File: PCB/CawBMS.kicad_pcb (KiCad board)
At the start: 4 copper layers, 53.5 x 38 mm, 132 parts, among them CN1 SWD, CN2 I2C, CN3 SPI, CN4 USART, CN5 SWD, CN6 WAFER-SH1.0-6PWB, Q1 CSD13381F4, Q10 TP0610K-T1-GE3, Q2 CSD13381F4, Q3 CSD13381F4, Q4 CSD13381F4, Q5 CSD13381F4, Q6 BSC0702LS, Q7 BSC0702LS, Q8 BSC0702LS, Q9 BSC0702LS, SW1 B3U-1000P, SW2 B3U-1000P, SW3 B3U-1000P, U1 STM32F103CBTx, U2 TCAN1044DRBRQ1, U3 TPS61240DRVR, U4 BQ7692003PW, U5 CAN, X1 Crystal_16MHz_15pF_3P

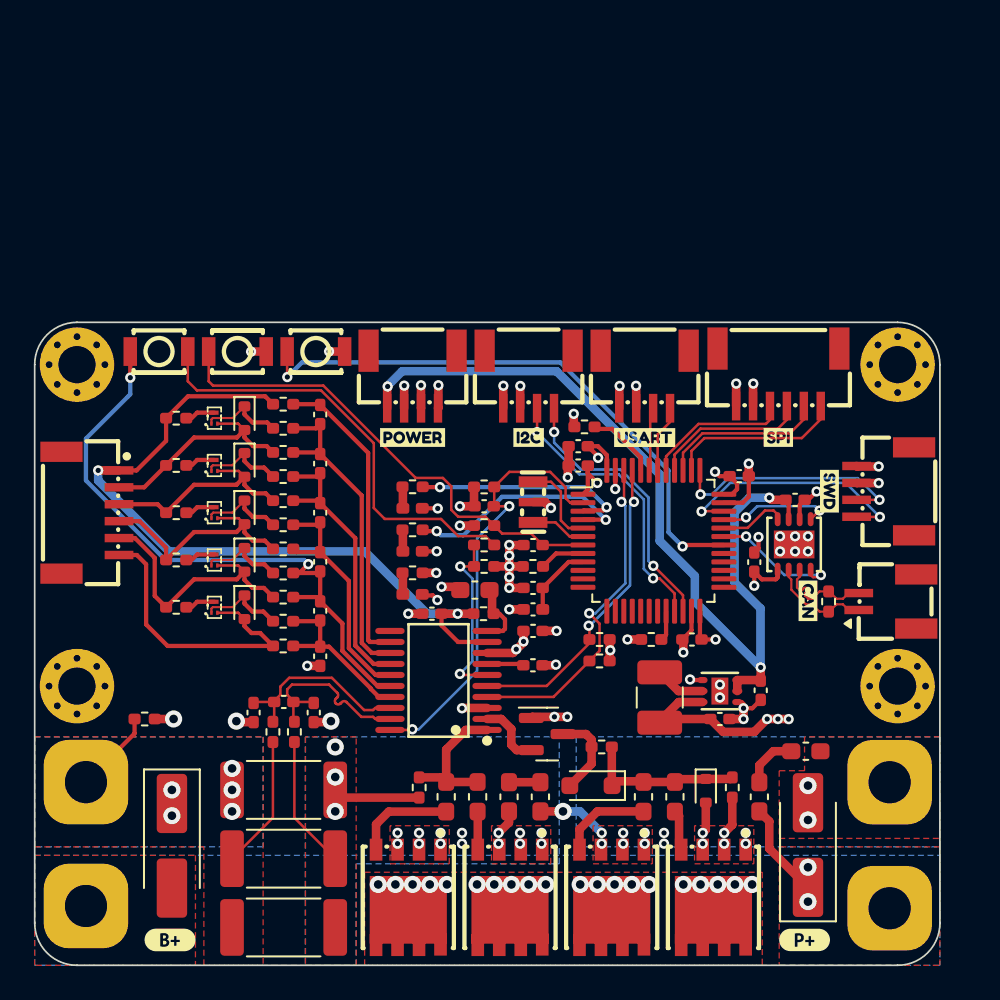
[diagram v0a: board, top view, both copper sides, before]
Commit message: feat(PCB): 新增预充功能; 支持2路电池温度采样; 支持低功耗模式; 更换主控芯片; 采用降压输出5V
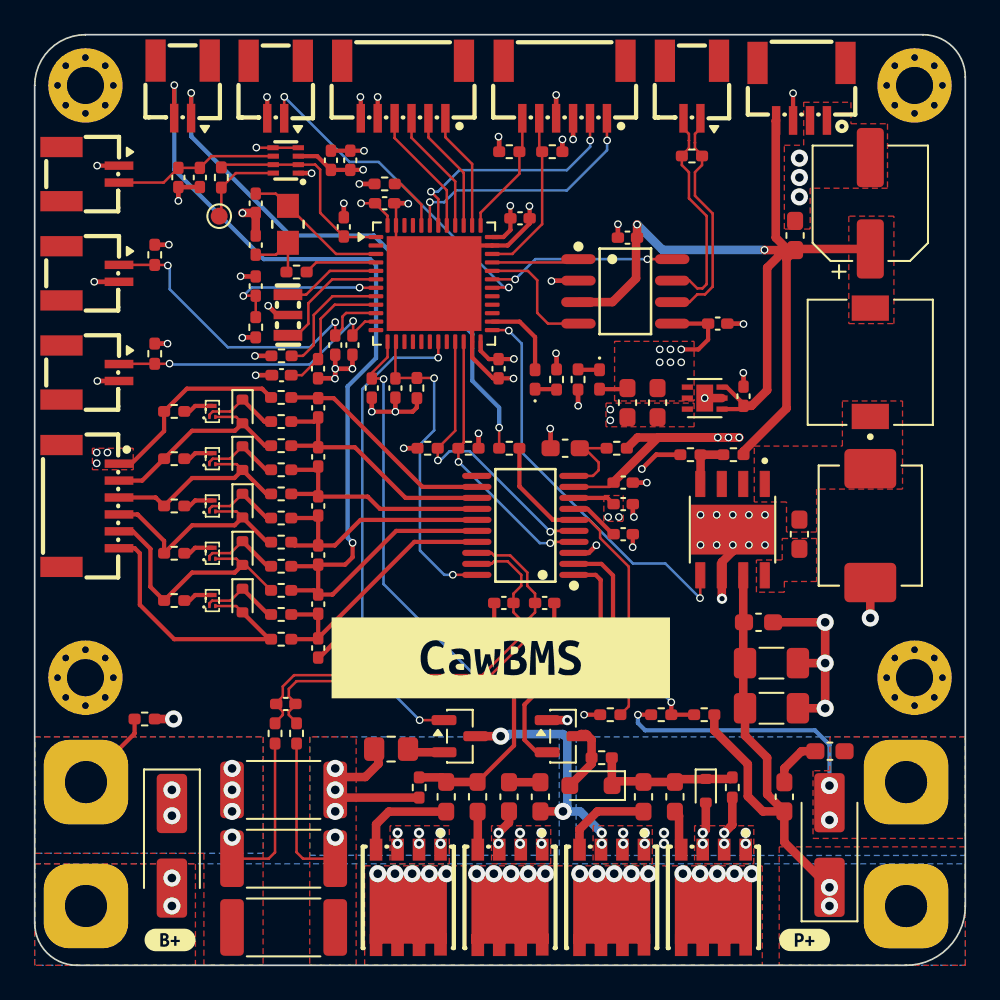
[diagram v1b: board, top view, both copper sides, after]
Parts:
- removed the C15 at (139.5, 110.2)
- removed the C16 at (150.5, 115.4)
- removed the C17 at (133.5, 109.2)
- removed the C24 at (136.6, 102.9)
- removed CN4: USART, Rick_Connector:CONN-SMD_4P-P1.00_WAFER-SH1.0-4PWB
- removed the CN5 at (160.3, 102.0)
- removed D3: LED, LED_SMD:LED_0402_1005Metric_Pad0.77x0.64mm_HandSolder
- removed G***: LOGO, Rick_Logo:guaik_logo_black_8x8
- removed the L2 at (146.9, 114.2)
- removed the R28 at (136.6, 106.4)
- removed the R29 at (136.6, 105.2)
- removed the R38 at (136.6, 101.7)
- removed REF**: OSHW-Logo2_9.8x8mm_SilkScreen, Symbol:OSHW-Logo2_9.8x8mm_SilkScreen
- removed SW1, SW2, SW3: B3U-1000P, Rick_Switch:B3U-1000P
- removed kibuzzard-6577EBAB: G***, kibuzzard-6577EBAB
- removed kibuzzard-6577EBC9: G***, kibuzzard-6577EBC9
- removed kibuzzard-6577EC0F: G***, kibuzzard-6577EC0F
- removed kibuzzard-6577EC47: G***, kibuzzard-6577EC47
- removed kibuzzard-6577F12B: G***, kibuzzard-6577F12B
- removed kibuzzard-6577F182: G***, kibuzzard-6577F182
- removed kibuzzard-6577F8B5: G***, kibuzzard-6577F8B5
- removed kibuzzard-658FE662: G***, kibuzzard-658FE662
- removed kibuzzard-658FE679: G***, kibuzzard-658FE679
- removed kibuzzard-65902364: G***, kibuzzard-65902364
- added C10: 0.1uF, Library:C_0402_1005Metric_Pad0.74x0.62mm_HandSolder, F.Cu at (150.4, 92.1)
- added C11: 0.1uF, Library:C_0402_1005Metric_Pad0.74x0.62mm_HandSolder, F.Cu at (123.1, 89.9)
- added C21: 10uF, Library:C_0603_1608Metric_Pad1.08x0.95mm_HandSolder, F.Cu at (141.4, 99.4)
- added C25: 470pF, Library:C_0402_1005Metric_Pad0.74x0.62mm_HandSolder, F.Cu at (131.3, 95.9)
- added C30: 4.7uF 50v, Library:C_1206_3216Metric_Pad1.33x1.80mm_HandSolder, F.Cu at (153.5, 114.8)
- added C31: 4.7uF 50v, Library:C_1206_3216Metric_Pad1.33x1.80mm_HandSolder, F.Cu at (153.5, 112.1)
- added C32: 0.01uF 50v, Library:C_0603_1608Metric_Pad1.08x0.95mm_HandSolder, F.Cu at (152.8, 109.7)
- added C33: 0.01uF, Library:C_0603_1608Metric_Pad1.08x0.95mm_HandSolder, F.Cu at (155.2, 104.5)
- added C34: 330uF, Library:CP_Elec_6.3x5.8, F.Cu at (159.4, 85.0)
- added C35: 0.01uF, Library:C_0603_1608Metric_Pad1.08x0.95mm_HandSolder, F.Cu at (154.9, 86.9)
- added C36: 0.1uF/50V, Library:C_0402_1005Metric_Pad0.74x0.62mm_HandSolder, F.Cu at (129.9, 95.9)
- added C37: 1uF, Library:C_0402_1005Metric_Pad0.74x0.62mm_HandSolder, F.Cu at (151.9, 96.4)
- added C38: 22uF, Library:C_0603_1608Metric_Pad1.08x0.95mm_HandSolder, F.Cu at (146.8, 96.7)
- added C39: 22uF, Library:C_0603_1608Metric_Pad1.08x0.95mm_HandSolder, F.Cu at (145.0, 96.7)
- added C40: 18pF, Library:C_0402_1005Metric_Pad0.74x0.62mm_HandSolder, F.Cu at (123.1, 85.0)
- added C41: 18pF, Library:C_0402_1005Metric_Pad0.74x0.62mm_HandSolder, F.Cu at (123.1, 87.4)
- added C42: 10uF, Library:C_0402_1005Metric_Pad0.74x0.62mm_HandSolder, F.Cu at (128.7, 82.4)
- added C43: 10uF, Library:C_0402_1005Metric_Pad0.74x0.62mm_HandSolder, F.Cu at (118.5, 83.4)
- added C44: 0.1uF, Library:C_0402_1005Metric_Pad0.74x0.62mm_HandSolder, F.Cu at (119.8, 83.4)
- added C9: 0.1uF, Library:C_0402_1005Metric_Pad0.74x0.62mm_HandSolder, F.Cu at (126.7, 94.7)
- added D13: B540C-13-F, Library:B540C-13-F, F.Cu at (159.4, 104.0)
- added IC1: LM66200DRLR, Library:LM66200DRLR, F.Cu at (124.8, 82.4)
- added L6: 15uH, Library:L_7.3x7.3_H3.5, F.Cu at (159.4, 94.4)
- added Q11: SI2308A, Library:SOT-23, F.Cu at (135.1, 116.5)
- added R11: 510, Library:R_0402_1005Metric_Pad0.72x0.64mm_HandSolder, F.Cu at (140.8, 95.4)
- added R13: 10k, Library:R_0402_1005Metric_Pad0.72x0.64mm_HandSolder, F.Cu at (123.1, 92.3)
- added R31: 10k, Library:R_0402_1005Metric_Pad0.72x0.64mm_HandSolder, F.Cu at (138.0, 99.4)
- added R32: 100, Library:R_0402_1005Metric_Pad0.72x0.64mm_HandSolder, F.Cu at (144.4, 99.4)
- added R39: 499k, Library:R_0402_1005Metric_Pad0.72x0.64mm_HandSolder, F.Cu at (132.6, 95.9)
- added R43: 10k 0.1%, Library:R_0402_1005Metric_Pad0.72x0.64mm_HandSolder, F.Cu at (151.3, 99.8)
- added R44: 3.16k 0.1%, Library:R_0402_1005Metric_Pad0.72x0.64mm_HandSolder, F.Cu at (148.8, 99.8)
- added R45: 100, Library:R_0805_2012Metric_Pad1.20x1.40mm_HandSolder, F.Cu at (131.1, 117.2)
- added R46: 10k, Library:R_0402_1005Metric_Pad0.72x0.64mm_HandSolder, F.Cu at (140.6, 81.9)
- added R47: 10k, Library:R_0402_1005Metric_Pad0.72x0.64mm_HandSolder, F.Cu at (138.0, 81.9)
- added R48: 75k 0.1%, Library:R_0402_1005Metric_Pad0.72x0.64mm_HandSolder, F.Cu at (149.6, 115.2)
- added R49: 3k 0.1%, Library:R_0402_1005Metric_Pad0.72x0.64mm_HandSolder, F.Cu at (147.0, 115.2)
- added TP1: TestPoint, Library:TestPoint_Pad_D1.0mm, F.Cu at (120.9, 85.7)
- added U10: KEY, Library:CONN-SMD_2P-P1.00_XUNPU_WAFER-SH1.0-2PWB, F.Cu at (124.2, 78.2)
- added U11: WAFER-SH1.0-2PWB, Library:CONN-SMD_2P-P1.00_XUNPU_WAFER-SH1.0-2PWB, F.Cu at (118.7, 78.2)
- added U12: KEY, Library:CONN-SMD_2P-P1.00_XUNPU_WAFER-SH1.0-2PWB, F.Cu at (113.3, 83.2)
- added U6: TJA1051T/3/1J, Library:TJA1051T31J_SOIC-8_L4.9-W3.9-P1.27-LS6.0-BL, F.Cu at (144.9, 90.2)
- added U8: TPS5450DDAR, Library:TPS5450DDAR, F.Cu at (151.2, 104.3)
- added U9: TLV76733DRVR, Library:TLV76733DRVR_SON65P200X200X80-7N, F.Cu at (149.6, 96.5)
- added XTAL1: Q13FC1350000400, Library:Q13FC1350000400, F.Cu at (125.0, 86.2)
- added kibuzzard-69A6F5A3: G***, Library:kibuzzard-69A6F5A3, F.Cu at (137.5, 111.8)
- C1, C2, C3, C4, C5, C6, C7, C8: footprint Capacitor_SMD:C_0402_1005Metric_Pad0.74x0.62mm_HandSolder -> Library:C_0402_1005Metric_Pad0.74x0.62mm_HandSolder
- C12: renamed from C9; footprint Capacitor_SMD:C_0402_1005Metric_Pad0.74x0.62mm_HandSolder -> Library:C_0402_1005Metric_Pad0.74x0.62mm_HandSolder
- C13: renamed from C10; footprint Capacitor_SMD:C_0402_1005Metric_Pad0.74x0.62mm_HandSolder -> Library:C_0402_1005Metric_Pad0.74x0.62mm_HandSolder
- C14: renamed from C11; footprint Capacitor_SMD:C_0402_1005Metric_Pad0.74x0.62mm_HandSolder -> Library:C_0402_1005Metric_Pad0.74x0.62mm_HandSolder
- C15: renamed from C12; footprint Capacitor_SMD:C_0402_1005Metric_Pad0.74x0.62mm_HandSolder -> Library:C_0402_1005Metric_Pad0.74x0.62mm_HandSolder
- C16: renamed from C13; footprint Capacitor_SMD:C_0402_1005Metric_Pad0.74x0.62mm_HandSolder -> Library:C_0402_1005Metric_Pad0.74x0.62mm_HandSolder
- C17: renamed from C14; footprint Capacitor_SMD:C_0402_1005Metric_Pad0.74x0.62mm_HandSolder -> Library:C_0402_1005Metric_Pad0.74x0.62mm_HandSolder
- C18: value 1uF -> 4.7uF; footprint Capacitor_SMD:C_0402_1005Metric_Pad0.74x0.62mm_HandSolder -> Library:C_0402_1005Metric_Pad0.74x0.62mm_HandSolder
- C19: value 10uF -> 1uF; footprint Capacitor_SMD:C_0603_1608Metric_Pad1.08x0.95mm_HandSolder -> Library:C_0402_1005Metric_Pad0.74x0.62mm_HandSolder
- C20: value 4.7uF -> 1uF; footprint Capacitor_SMD:C_0402_1005Metric_Pad0.74x0.62mm_HandSolder -> Library:C_0402_1005Metric_Pad0.74x0.62mm_HandSolder
- C22: renamed from C21; footprint Capacitor_SMD:C_0402_1005Metric_Pad0.74x0.62mm_HandSolder -> Library:C_0402_1005Metric_Pad0.74x0.62mm_HandSolder
- C23: renamed from C22; footprint Capacitor_SMD:C_0402_1005Metric_Pad0.74x0.62mm_HandSolder -> Library:C_0402_1005Metric_Pad0.74x0.62mm_HandSolder
- C24: renamed from C23; footprint Capacitor_SMD:C_0402_1005Metric_Pad0.74x0.62mm_HandSolder -> Library:C_0402_1005Metric_Pad0.74x0.62mm_HandSolder
- C26: renamed from C25; footprint Capacitor_SMD:C_0603_1608Metric_Pad1.08x0.95mm_HandSolder -> Library:C_0603_1608Metric_Pad1.08x0.95mm_HandSolder
- C27: renamed from C26; footprint Capacitor_SMD:C_0603_1608Metric_Pad1.08x0.95mm_HandSolder -> Library:C_0603_1608Metric_Pad1.08x0.95mm_HandSolder
- C28: renamed from C27; footprint Capacitor_SMD:C_0603_1608Metric_Pad1.08x0.95mm_HandSolder -> Library:C_0603_1608Metric_Pad1.08x0.95mm_HandSolder
- C29: renamed from C28; footprint Capacitor_SMD:C_0603_1608Metric_Pad1.08x0.95mm_HandSolder -> Library:C_0603_1608Metric_Pad1.08x0.95mm_HandSolder
- CN1: renamed from CN3; footprint Rick_Connector:CONN-SMD_6P-P1.00_XUNPU_WAFER-SH1.0-6PWB -> Library:CONN-SMD_6P-P1.00_XUNPU_WAFER-SH1.0-6PWB
- CN2: value I2C -> WAFER-SH1.0-6PWB; footprint Rick_Connector:CONN-SMD_4P-P1.00_WAFER-SH1.0-4PWB -> Library:CONN-SMD_6P-P1.00_XUNPU_WAFER-SH1.0-6PWB
- CN5: renamed from CN1; footprint Rick_Connector:CONN-SMD_4P-P1.00_WAFER-SH1.0-4PWB -> Library:CONN-SMD_4P-P1.00_WAFER-SH1.0-4PWB
- CN6: footprint Rick_Connector:CONN-SMD_6P-P1.00_XUNPU_WAFER-SH1.0-6PWB -> Library:CONN-SMD_6P-P1.00_XUNPU_WAFER-SH1.0-6PWB
- D1, D2: footprint LED_SMD:LED_0402_1005Metric_Pad0.77x0.64mm_HandSolder -> Library:LED_0402_1005Metric_Pad0.77x0.64mm_HandSolder
- D10: renamed from D12; footprint Diode_SMD:D_SOD-523 -> Library:D_SOD-523
- D11: renamed from D10; footprint Diode_SMD:D_SMA_Handsoldering -> Library:D_SMA_Handsoldering
- D12: renamed from D9; footprint Diode_SMD:D_SMA_Handsoldering -> Library:D_SMA_Handsoldering
- D4, D5, D6, D7, D8: footprint Diode_SMD:D_SOD-523 -> Library:D_SOD-523
- D9: renamed from D11; footprint Diode_SMD:D_SOD-323_HandSoldering -> Library:D_SOD-323_HandSoldering
- H1, H2, H3, H4: footprint MountingHole:MountingHole_2.2mm_M2_Pad_Via -> Library:MountingHole_2.2mm_M2_Pad_Via
- H5: renamed from H7; footprint CawBMS:POWER_PAD -> Library:POWER_PAD
- H6: renamed from H8; footprint CawBMS:POWER_PAD -> Library:POWER_PAD
- H7: renamed from H5; footprint CawBMS:POWER_PAD -> Library:POWER_PAD
- H8: renamed from H6; footprint CawBMS:POWER_PAD -> Library:POWER_PAD
- L1: footprint Inductor_SMD:L_0402_1005Metric_Pad0.77x0.64mm_HandSolder -> Library:L_0402_1005Metric_Pad0.77x0.64mm_HandSolder
- L2: renamed from L3; footprint Inductor_SMD:L_0603_1608Metric_Pad1.05x0.95mm_HandSolder -> Library:L_0603_1608Metric_Pad1.05x0.95mm_HandSolder
- L3: renamed from L4; footprint Inductor_SMD:L_0603_1608Metric_Pad1.05x0.95mm_HandSolder -> Library:L_0603_1608Metric_Pad1.05x0.95mm_HandSolder
- L4: renamed from L5; footprint Inductor_SMD:L_0603_1608Metric_Pad1.05x0.95mm_HandSolder -> Library:L_0603_1608Metric_Pad1.05x0.95mm_HandSolder
- L5: renamed from L6; footprint Inductor_SMD:L_0603_1608Metric_Pad1.05x0.95mm_HandSolder -> Library:L_0603_1608Metric_Pad1.05x0.95mm_HandSolder
- Q1, Q2, Q3, Q4, Q5: footprint Rick_MOSFET:CSD13381F4_PICOSTAR-3_L1.0-W0.6-P0.40-S0.65-BL-1 -> Library:CSD13381F4_PICOSTAR-3_L1.0-W0.6-P0.40-S0.65-BL-1
- Q10: renamed from Q9; footprint Rick_MOSFET:BSC0702LS_PG-TDSON-8_L5.0-W6.0-P1.27-BL-EP -> Library:BSC0702LS_PG-TDSON-8_L5.0-W6.0-P1.27-BL-EP
- Q6, Q7: footprint Rick_MOSFET:BSC0702LS_PG-TDSON-8_L5.0-W6.0-P1.27-BL-EP -> Library:BSC0702LS_PG-TDSON-8_L5.0-W6.0-P1.27-BL-EP
- Q8: renamed from Q10; footprint Package_TO_SOT_SMD:SOT-23 -> Library:SOT-23
- Q9: renamed from Q8; footprint Rick_MOSFET:BSC0702LS_PG-TDSON-8_L5.0-W6.0-P1.27-BL-EP -> Library:BSC0702LS_PG-TDSON-8_L5.0-W6.0-P1.27-BL-EP
- R1, R4: value 10k -> 10k 0.1%; footprint Resistor_SMD:R_0402_1005Metric_Pad0.72x0.64mm_HandSolder -> Library:R_0402_1005Metric_Pad0.72x0.64mm_HandSolder
- R10, R8: footprint Resistor_SMD:R_0402_1005Metric_Pad0.72x0.64mm_HandSolder -> Library:R_0402_1005Metric_Pad0.72x0.64mm_HandSolder
- R14: renamed from R12; footprint Resistor_SMD:R_0402_1005Metric_Pad0.72x0.64mm_HandSolder -> Library:R_0402_1005Metric_Pad0.72x0.64mm_HandSolder
- R15: renamed from R13; footprint Resistor_SMD:R_0402_1005Metric_Pad0.72x0.64mm_HandSolder -> Library:R_0402_1005Metric_Pad0.72x0.64mm_HandSolder
- R16: renamed from R14; footprint Resistor_SMD:R_0402_1005Metric_Pad0.72x0.64mm_HandSolder -> Library:R_0402_1005Metric_Pad0.72x0.64mm_HandSolder
- R17: renamed from R15; footprint Resistor_SMD:R_0402_1005Metric_Pad0.72x0.64mm_HandSolder -> Library:R_0402_1005Metric_Pad0.72x0.64mm_HandSolder
- R18: renamed from R16; footprint Resistor_SMD:R_0402_1005Metric_Pad0.72x0.64mm_HandSolder -> Library:R_0402_1005Metric_Pad0.72x0.64mm_HandSolder
- R19: renamed from R17; footprint Resistor_SMD:R_0402_1005Metric_Pad0.72x0.64mm_HandSolder -> Library:R_0402_1005Metric_Pad0.72x0.64mm_HandSolder
- R2, R5: value 10k -> 0; footprint Resistor_SMD:R_0402_1005Metric_Pad0.72x0.64mm_HandSolder -> Library:R_0402_1005Metric_Pad0.72x0.64mm_HandSolder
- R20: renamed from R18; footprint Resistor_SMD:R_0402_1005Metric_Pad0.72x0.64mm_HandSolder -> Library:R_0402_1005Metric_Pad0.72x0.64mm_HandSolder
- R21: renamed from R19; footprint Resistor_SMD:R_0402_1005Metric_Pad0.72x0.64mm_HandSolder -> Library:R_0402_1005Metric_Pad0.72x0.64mm_HandSolder
- R22: renamed from R20; footprint Resistor_SMD:R_0402_1005Metric_Pad0.72x0.64mm_HandSolder -> Library:R_0402_1005Metric_Pad0.72x0.64mm_HandSolder
- R23: renamed from R21; footprint Resistor_SMD:R_0402_1005Metric_Pad0.72x0.64mm_HandSolder -> Library:R_0402_1005Metric_Pad0.72x0.64mm_HandSolder
- R24: renamed from R22; footprint Resistor_SMD:R_0402_1005Metric_Pad0.72x0.64mm_HandSolder -> Library:R_0402_1005Metric_Pad0.72x0.64mm_HandSolder
- R25: renamed from R23; footprint Resistor_SMD:R_0402_1005Metric_Pad0.72x0.64mm_HandSolder -> Library:R_0402_1005Metric_Pad0.72x0.64mm_HandSolder
- R26: renamed from R24; footprint Resistor_SMD:R_0402_1005Metric_Pad0.72x0.64mm_HandSolder -> Library:R_0402_1005Metric_Pad0.72x0.64mm_HandSolder
- R27: renamed from R25; footprint Resistor_SMD:R_0402_1005Metric_Pad0.72x0.64mm_HandSolder -> Library:R_0402_1005Metric_Pad0.72x0.64mm_HandSolder
- R28: renamed from R26; footprint Resistor_SMD:R_0402_1005Metric_Pad0.72x0.64mm_HandSolder -> Library:R_0402_1005Metric_Pad0.72x0.64mm_HandSolder
- R29: renamed from R27; footprint Resistor_SMD:R_0402_1005Metric_Pad0.72x0.64mm_HandSolder -> Library:R_0402_1005Metric_Pad0.72x0.64mm_HandSolder
- R3: value 0 -> 10k; footprint Resistor_SMD:R_0402_1005Metric_Pad0.72x0.64mm_HandSolder -> Library:R_0402_1005Metric_Pad0.72x0.64mm_HandSolder
- R30: value 100 -> NTC 10k; footprint Resistor_SMD:R_0402_1005Metric_Pad0.72x0.64mm_HandSolder -> Library:R_0402_1005Metric_Pad0.72x0.64mm_HandSolder
- R33: renamed from R31; footprint Resistor_SMD:R_0402_1005Metric_Pad0.72x0.64mm_HandSolder -> Library:R_0402_1005Metric_Pad0.72x0.64mm_HandSolder
- R34: renamed from R32; footprint Resistor_SMD:R_2512_6332Metric_Pad1.40x3.35mm_HandSolder -> Library:R_2512_6332Metric_Pad1.40x3.35mm_HandSolder
- R35: renamed from R33; footprint Resistor_SMD:R_2512_6332Metric_Pad1.40x3.35mm_HandSolder -> Library:R_2512_6332Metric_Pad1.40x3.35mm_HandSolder
- R36: renamed from R34; footprint Resistor_SMD:R_2512_6332Metric_Pad1.40x3.35mm_HandSolder -> Library:R_2512_6332Metric_Pad1.40x3.35mm_HandSolder
- R37: renamed from R35; footprint Resistor_SMD:R_0402_1005Metric_Pad0.72x0.64mm_HandSolder -> Library:R_0402_1005Metric_Pad0.72x0.64mm_HandSolder
- R38: renamed from R36; footprint Resistor_SMD:R_0402_1005Metric_Pad0.72x0.64mm_HandSolder -> Library:R_0402_1005Metric_Pad0.72x0.64mm_HandSolder
- R40: renamed from R39; footprint Resistor_SMD:R_0402_1005Metric_Pad0.72x0.64mm_HandSolder -> Library:R_0402_1005Metric_Pad0.72x0.64mm_HandSolder
- R41: renamed from R40; footprint Resistor_SMD:R_0402_1005Metric_Pad0.72x0.64mm_HandSolder -> Library:R_0402_1005Metric_Pad0.72x0.64mm_HandSolder
- R42: renamed from R37; footprint Resistor_SMD:R_0402_1005Metric_Pad0.72x0.64mm_HandSolder -> Library:R_0402_1005Metric_Pad0.72x0.64mm_HandSolder
- R6: value 120 -> 10K; footprint Resistor_SMD:R_0402_1005Metric_Pad0.72x0.64mm_HandSolder -> Library:R_0402_1005Metric_Pad0.72x0.64mm_HandSolder
- R7: value 510 -> 10k; footprint Resistor_SMD:R_0402_1005Metric_Pad0.72x0.64mm_HandSolder -> Library:R_0402_1005Metric_Pad0.72x0.64mm_HandSolder
- R9: value 510 -> 120Ω 1%; footprint Resistor_SMD:R_0402_1005Metric_Pad0.72x0.64mm_HandSolder -> Library:R_0402_1005Metric_Pad0.72x0.64mm_HandSolder
- U1: value STM32F103CBTx -> WAFER-SH1.0-2PWB; footprint Package_QFP:LQFP-48_7x7mm_P0.5mm -> Library:CONN-SMD_2P-P1.00_XUNPU_WAFER-SH1.0-2PWB
- U2: value TCAN1044DRBRQ1 -> WAFER-SH1.0-2PWB; footprint Rick_CAN:TCAN1044DRBRQ1_DFN-8_L3.0-W3.0-P0.65-TL-EP2.4 -> Library:CONN-SMD_2P-P1.00_XUNPU_WAFER-SH1.0-2PWB
- U3: value TPS61240DRVR -> STM32L431CCUx; footprint Rick_DC-DC:TPS61240DRVR_WSON-6_L2.0-W2.0-P0.65-TL-EP -> Library:QFN-48-1EP_7x7mm_P0.5mm_EP5.6x5.6mm
- U5: footprint Rick_Connector:CONN-SMD_2P-P1.00_XUNPU_WAFER-SH1.0-2PWB -> Library:CONN-SMD_2P-P1.00_XUNPU_WAFER-SH1.0-2PWB
- U7: renamed from U4; footprint Rick_BMS:BQ7692003PW_TSSOP-20_L6.5-W4.4-P0.65-LS6.4-BL -> Library:BQ7692003PW_TSSOP-20_L6.5-W4.4-P0.65-LS6.4-BL
- X1: footprint Rick_Crystal:Crystal_SMD3213-3P -> Library:Crystal_SMD3213-3P
- kibuzzard-6582907D: footprint kibuzzard-6582907D -> Library:kibuzzard-6582907D
- kibuzzard-65829086: footprint kibuzzard-65829086 -> Library:kibuzzard-65829086
- moved R6 43.8 mm to (121.0, 83.4)
- moved U2 42.8 mm to (113.3, 95.0)
- moved R1 37.1 mm to (117.1, 88.0), turned to 90 degrees
- moved U1 36.8 mm to (113.3, 89.1), turned to -90 degrees
- moved U5 32.4 mm to (148.8, 78.2), turned to 180 degrees
- moved R4 31.2 mm to (117.1, 93.9), turned to 90 degrees
- moved C3 30.5 mm to (127.5, 82.4), turned to -90 degrees
- moved C7 30.4 mm to (130.7, 85.0), turned to 0 degrees
- moved U3 29.4 mm to (133.6, 89.7), turned to 0 degrees
- moved CN5 28.6 mm to (155.3, 78.4)
- moved CN1 28.0 mm to (131.8, 78.2)
- moved R9 27.6 mm to (148.8, 82.2), turned to 180 degrees
- moved C2 26.6 mm to (128.8, 93.3), turned to 90 degrees
- moved R5 26.0 mm to (124.6, 94.0)
- moved R3 24.2 mm to (130.7, 83.8), turned to 0 degrees
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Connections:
- C1 pad 1: +3.3V -> GND
- C1 pad 2: GND -> /ADC1_IN5
- C18 pad 1: GND -> +3.3V
- C18 pad 2: Net-(U4-CAP1) -> GND
- C19 pad 1: Net-(U4-BAT) -> /BQ76920/BAT
- C2 pad 1: +3.3V -> GND
- C2 pad 2: GND -> /ADC1_IN6
- C20 pad 1: +5V -> GND
- C20 pad 2: GND -> Net-(U7-CAP1)
- C22 pad 2: /BQ76920/SRP -> /BQ76920/SRN
- C23 pad 1: /BQ76920/SRP -> /BQ76920/SRN
- C23 pad 2: /BQ76920/SRN -> /BQ76920/SRP
- C24 pad 1: /BQ76920/SRN -> /BQ76920/SRP
- C3 pad 1: +3.3V -> GND
- C3 pad 2: GND -> +3.3V
- C4 pad 1: +3.3V -> /VBAT
- C5 pad 1: +5V -> +3.3V
- C6 pad 1: +3.3VA -> +3.3V
- C8 pad 1: /RESET -> +5V
- CN1 pad 6: +3.3V -> +3V3
- CN2 pad 1: /I2C2_SDA -> /USART1_RX
- CN2 pad 2: /I2C2_SCL -> /USART1_TX
- CN2 pad 3: GND -> +3.3V
- CN2 pad 4: +3.3V -> GND
- CN2 pad 5: unconnected-(CN2-Pad5) -> /SWDIO
- CN2 pad 6: unconnected-(CN2-Pad6) -> /SWCLK
- CN5 pad 3: +3.3V -> +3V3
- D1 pad 2: +3.3V -> +3V3
- D2 pad 2: +3.3V -> /STA_LED
- R1 pad 1: GND -> /ADC1_IN5
- R1 pad 2: Net-(U1-PB2) -> +3V3
- R10 pad 1: Net-(D3-K) -> Net-(D1-K)
- R2 pad 1: GND -> Net-(C41-Pad1)
- R2 pad 2: Net-(U1-BOOT0) -> /RCC_OSC32_OUT
- R3 pad 1: Net-(U1-VSSA) -> GND
- R3 pad 2: GND -> Net-(U3-PH3)
- R30 pad 1: /BQ76920/BAT -> GND
- R30 pad 2: Net-(U4-BAT) -> Net-(U7-TS1)
- R33 pad 2: /BQ76920/SRP -> /BQ76920/SRN
- R37 pad 2: /BQ76920/SRN -> /BQ76920/SRP
- R4 pad 1: +3.3V -> /ADC1_IN6
- R4 pad 2: /I2C1_SCL -> +3V3
- R5 pad 1: +3.3V -> Net-(U3-VSSA)
- R5 pad 2: /I2C1_SDA -> GND
- R6 pad 1: /CAN_N -> Net-(IC1-ST)
- R6 pad 2: /CAN_P -> /VBAT
- R7 pad 1: Net-(D1-K) -> +3.3V
- R7 pad 2: /LED_A -> /I2C2_SCL
- R8 pad 2: /RESET -> /I2C2_SDA
- R9 pad 1: Net-(D2-K) -> /CAN_N
- R9 pad 2: /LED_B -> /CAN_P
- U1 pad 1: +3.3V -> /ADC1_IN5
- U1 pad 2: /ALERT -> GND
- U1 pad 3: /LED_A -> unconnected-(U1-Pad3)
- U1 pad 4: /LED_B -> unconnected-(U1-Pad4)
- U2 pad 1: /CAN_TX -> /ADC1_IN6
- U2 pad 3: +5V -> unconnected-(U2-Pad3)
- U2 pad 4: /CAN_RX -> unconnected-(U2-Pad4)
- U3 pad 1: GND -> /VBAT
- U3 pad 2: +5V -> unconnected-(U3-PC13-Pad2)
- U3 pad 3: +5V -> /RCC_OSC32_IN
- U3 pad 4: +3.3V -> /RCC_OSC32_OUT
- U3 pad 5: Net-(U3-L) -> /HSE_IN
- U3 pad 6: +3.3V -> /HSE_OUT
- U3 pad 7: GND -> /RESET
- U7 pad 10: Net-(U4-BAT) -> Net-(U7-BAT)
- U7 pad 4: /I2C1_SDA -> /I2C2_SDA
- U7 pad 5: /I2C1_SCL -> /I2C2_SCL
- U7 pad 6: Net-(U4-TS1) -> Net-(U7-TS1)
- U7 pad 7: Net-(U4-CAP1) -> Net-(U7-CAP1)
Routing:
- net GND: track 48.4 -> 86.7 mm, vias 45 -> 64
- net /ADC1_IN8: track 0.00 -> 37.4 mm, vias 0 -> 2
- net Net-(R31-Pad1): track 0.00 -> 32.9 mm, vias 0 -> 2
- net /EN_PRE_CHARGE: track 0.00 -> 28.6 mm, vias 0 -> 2
- net Net-(R29-Pad1): track 26.1 -> 0.00 mm
- net PACK-: track 8.30 -> 33.8 mm, vias 17 -> 19
- net /5V_EN: track 0.00 -> 24.0 mm, vias 0 -> 2
- net PACK+: track 5.68 -> 28.6 mm, vias 2 -> 4
- net +3.3V: track 42.2 -> 19.9 mm, vias 22 -> 12
- net /ADC1_IN5: track 0.00 -> 20.3 mm, vias 0 -> 2
- net /BQ76920/VC1: track 37.2 -> 57.4 mm
- net /I2C1_SDA: track 20.0 -> 0.00 mm, vias 2 -> 0
- net Net-(U7-TS1): track 0.00 -> 19.9 mm
- net /RESET: track 28.7 -> 10.1 mm, vias 0 -> 2
- net /I2C1_SCL: track 18.5 -> 0.00 mm, vias 2 -> 0
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- added copper zone on F.Cu, net +3.3V
- added copper zone on F.Cu, net +3V3
- added copper zone on In2.Cu, net +3V3
- added copper zone on F.Cu, net +5V
- added copper zone on F.Cu, net /BQ76920/BAT
- added copper zone on In2.Cu, net /BQ76920/BAT
- added copper zone on F.Cu, net GND
- added copper zone on F.Cu, net Net-(U8-BOOT)
- added copper zone on F.Cu, net Net-(U8-PH)
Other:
- board size 53.5 x 38 mm -> 55 x 55 mm

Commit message: fix(PCB): 调优放电/预充电阻功率与母线采样布局
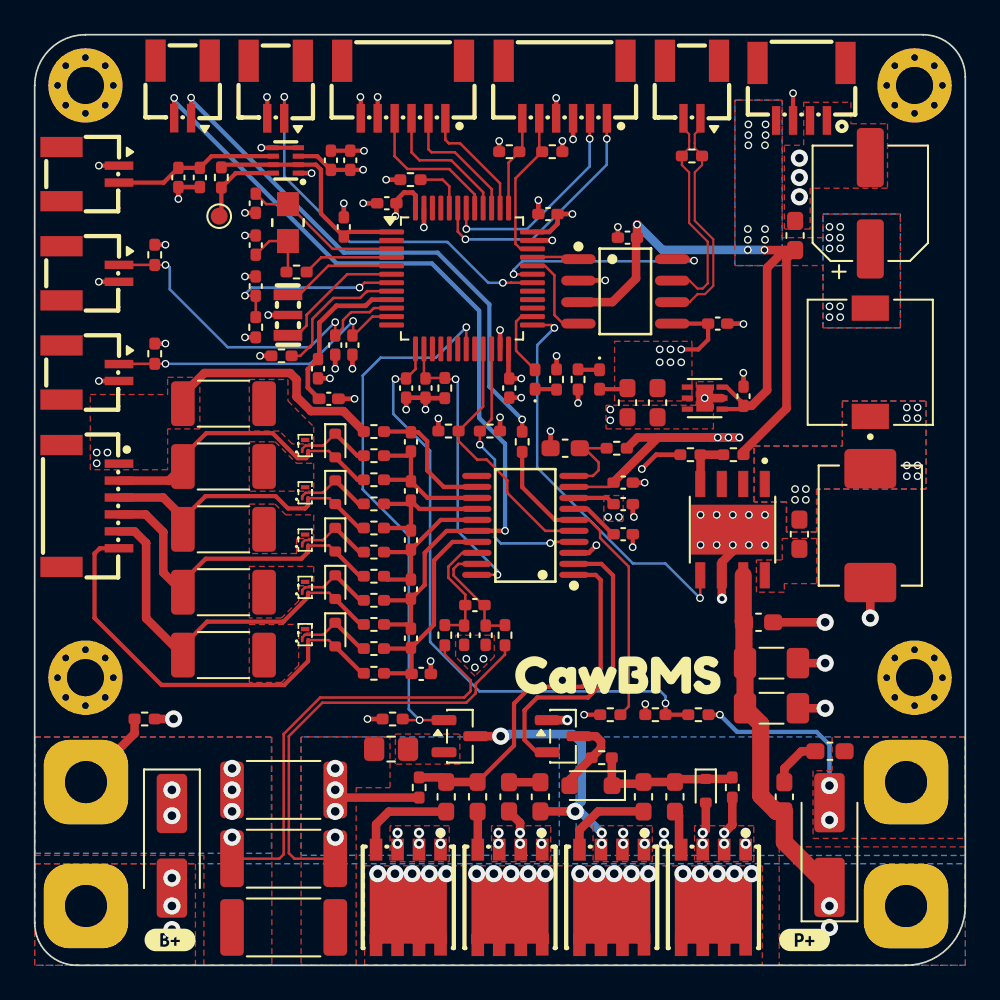
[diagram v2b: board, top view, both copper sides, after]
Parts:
- removed U3: STM32L431CCUx, Library:QFN-48-1EP_7x7mm_P0.5mm_EP5.6x5.6mm
- removed kibuzzard-69A6F5A3: G***, Library:kibuzzard-69A6F5A3
- added R12: 10k, Resistor_SMD:R_0402_1005Metric_Pad0.72x0.64mm_HandSolder, F.Cu at (131.2, 115.4)
- added REF**: ESD-Logo_13.2x12mm_SilkScreen, Symbol:ESD-Logo_13.2x12mm_SilkScreen, B.Cu at (137.5, 95.5)
- added U4: STM32L431CCTx, Package_QFP:LQFP-48_7x7mm_P0.5mm, F.Cu at (135.3, 89.4)
- added kibuzzard-69B05E76: G***, kibuzzard-69B05E76, B.Cu at (137.5, 111.7)
- added kibuzzard-69B5918C: G***, kibuzzard-69B5918C, F.Cu at (144.5, 112.9)
- C1, C10, C11, C12, C13, C14, C15, C16, C17, C18, C2, C25, C3, C37, C4, C40, C41, C42, C43, C44, C5, C6, C7, C8, C9: footprint Library:C_0402_1005Metric_Pad0.74x0.62mm_HandSolder -> Capacitor_SMD:C_0402_1005Metric_Pad0.74x0.62mm_HandSolder
- C19, C20: value 1uF -> 1uF 50V; footprint Library:C_0402_1005Metric_Pad0.74x0.62mm_HandSolder -> Capacitor_SMD:C_0402_1005Metric_Pad0.74x0.62mm_HandSolder
- C21: value 10uF -> 10uF 50V; footprint Library:C_0603_1608Metric_Pad1.08x0.95mm_HandSolder -> Capacitor_SMD:C_0603_1608Metric_Pad1.08x0.95mm_HandSolder
- C22, C23, C24: value 0.1uF -> 0.1uF 50V; footprint Library:C_0402_1005Metric_Pad0.74x0.62mm_HandSolder -> Capacitor_SMD:C_0402_1005Metric_Pad0.74x0.62mm_HandSolder
- C26, C27, C28, C29: value 0.1uF -> 0.1uF 50V; footprint Library:C_0603_1608Metric_Pad1.08x0.95mm_HandSolder -> Capacitor_SMD:C_0603_1608Metric_Pad1.08x0.95mm_HandSolder
- C30, C31: value 4.7uF 50v -> 4.7uF 50V; footprint Library:C_1206_3216Metric_Pad1.33x1.80mm_HandSolder -> Capacitor_SMD:C_1206_3216Metric_Pad1.33x1.80mm_HandSolder
- C32: value 0.01uF 50v -> 0.01uF 50V; footprint Library:C_0603_1608Metric_Pad1.08x0.95mm_HandSolder -> Capacitor_SMD:C_0603_1608Metric_Pad1.08x0.95mm_HandSolder
- C33, C35, C38, C39: footprint Library:C_0603_1608Metric_Pad1.08x0.95mm_HandSolder -> Capacitor_SMD:C_0603_1608Metric_Pad1.08x0.95mm_HandSolder
- C34: value 330uF -> HV1C337M0607PZ; footprint Library:CP_Elec_6.3x5.8 -> Capacitor_SMD:CP_Elec_6.3x5.8
- C36: value 0.1uF/50V -> 0.1uF 50V; footprint Library:C_0402_1005Metric_Pad0.74x0.62mm_HandSolder -> Capacitor_SMD:C_0402_1005Metric_Pad0.74x0.62mm_HandSolder
- CN1: value SPI -> WAFER-SH1.0-6PWB; footprint Library:CONN-SMD_6P-P1.00_XUNPU_WAFER-SH1.0-6PWB -> Rick_Connector:CONN-SMD_6P-P1.00_XUNPU_WAFER-SH1.0-6PWB
- CN2, CN6: footprint Library:CONN-SMD_6P-P1.00_XUNPU_WAFER-SH1.0-6PWB -> Rick_Connector:CONN-SMD_6P-P1.00_XUNPU_WAFER-SH1.0-6PWB
- CN5: value SWD -> WAFER-SH1.0-4PWB; footprint Library:CONN-SMD_4P-P1.00_WAFER-SH1.0-4PWB -> Rick_Connector:CONN-SMD_4P-P1.00_WAFER-SH1.0-4PWB
- D1: value LED -> PWR_LED; footprint Library:LED_0402_1005Metric_Pad0.77x0.64mm_HandSolder -> LED_SMD:LED_0402_1005Metric_Pad0.77x0.64mm_HandSolder
- D10: value D_Zener_16V -> BZX585-B16,115; footprint Library:D_SOD-523 -> Diode_SMD:D_SOD-523
- D11: value D_200V -> ES1D; footprint Library:D_SMA_Handsoldering -> Diode_SMD:D_SMA_Handsoldering
- D12: value TVS_24V -> SMAJ24CA; footprint Library:D_SMA_Handsoldering -> Diode_SMD:D_SMA_Handsoldering
- D13: footprint Library:B540C-13-F -> Rick_Diode:B540C-13-F
- D2: value LED -> STA_LED; footprint Library:LED_0402_1005Metric_Pad0.77x0.64mm_HandSolder -> LED_SMD:LED_0402_1005Metric_Pad0.77x0.64mm_HandSolder
- D4, D5, D6, D7, D8: value D_Zener_5.6V -> EDZVT2R5.6B; footprint Library:D_SOD-523 -> Diode_SMD:D_SOD-523
- D9: value D_100V -> 1N4148WS T4; footprint Library:D_SOD-323_HandSoldering -> Diode_SMD:D_SOD-323_HandSoldering
- H1, H2, H3, H4: footprint Library:MountingHole_2.2mm_M2_Pad_Via -> MountingHole:MountingHole_2.2mm_M2_Pad_Via
- H5, H6, H7, H8: footprint Library:POWER_PAD -> CawBMS:POWER_PAD
- IC1: footprint Library:LM66200DRLR -> Rick_Diode:LM66200DRLR
- L1: footprint Library:L_0402_1005Metric_Pad0.77x0.64mm_HandSolder -> Inductor_SMD:L_0402_1005Metric_Pad0.77x0.64mm_HandSolder
- L2, L3, L4, L5: value 220ohm -> BLM18EG221SN1D; footprint Library:L_0603_1608Metric_Pad1.05x0.95mm_HandSolder -> Inductor_SMD:L_0603_1608Metric_Pad1.05x0.95mm_HandSolder
- L6: value 15uH -> ZEMS0650-150M; footprint Library:L_7.3x7.3_H3.5 -> Inductor_SMD:L_7.3x7.3_H3.5
- Q1, Q2, Q3, Q4, Q5: footprint Library:CSD13381F4_PICOSTAR-3_L1.0-W0.6-P0.40-S0.65-BL-1 -> Rick_MOSFET:CSD13381F4_PICOSTAR-3_L1.0-W0.6-P0.40-S0.65-BL-1
- Q10, Q6, Q7, Q9: footprint Library:BSC0702LS_PG-TDSON-8_L5.0-W6.0-P1.27-BL-EP -> Rick_MOSFET:BSC0702LS_PG-TDSON-8_L5.0-W6.0-P1.27-BL-EP
- Q11: value SI2308A -> AO3400A; footprint Library:SOT-23 -> Package_TO_SOT_SMD:SOT-23
- Q8: footprint Library:SOT-23 -> Package_TO_SOT_SMD:SOT-23
- R1, R10, R11, R13, R19, R2, R20, R21, R22, R23, R24, R25, R26, R27, R28, R29, R3, R31, R32, R38, R39, R4, R40, R41, R42, R43, R44, R46, R47, R48, R49, R5, R7, R8, R9: footprint Library:R_0402_1005Metric_Pad0.72x0.64mm_HandSolder -> Resistor_SMD:R_0402_1005Metric_Pad0.72x0.64mm_HandSolder
- R14, R15, R16, R17, R18: footprint Library:R_0402_1005Metric_Pad0.72x0.64mm_HandSolder -> Resistor_SMD:R_2010_5025Metric_Pad1.40x2.65mm_HandSolder
- R30: value NTC 10k -> NCP15XH103F03RC; footprint Library:R_0402_1005Metric_Pad0.72x0.64mm_HandSolder -> Resistor_SMD:R_0402_1005Metric_Pad0.72x0.64mm_HandSolder
- R33, R37: value 100 -> 100 0.1%; footprint Library:R_0402_1005Metric_Pad0.72x0.64mm_HandSolder -> Resistor_SMD:R_0402_1005Metric_Pad0.72x0.64mm_HandSolder
- R34, R35, R36: value 0.0015 -> HoJLRX2512-2W-1.5mR-1%; footprint Library:R_2512_6332Metric_Pad1.40x3.35mm_HandSolder -> Resistor_SMD:R_2512_6332Metric_Pad1.40x3.35mm_HandSolder
- R45: footprint Library:R_0805_2012Metric_Pad1.20x1.40mm_HandSolder -> Resistor_SMD:R_0805_2012Metric_Pad1.20x1.40mm_HandSolder
- R6: value 10K -> 10k; footprint Library:R_0402_1005Metric_Pad0.72x0.64mm_HandSolder -> Resistor_SMD:R_0402_1005Metric_Pad0.72x0.64mm_HandSolder
- TP1: footprint Library:TestPoint_Pad_D1.0mm -> TestPoint:TestPoint_Pad_D1.0mm
- U1, U11, U2: footprint Library:CONN-SMD_2P-P1.00_XUNPU_WAFER-SH1.0-2PWB -> Rick_Connector:CONN-SMD_2P-P1.00_XUNPU_WAFER-SH1.0-2PWB
- U10, U12: value KEY -> WAFER-SH1.0-2PWB; footprint Library:CONN-SMD_2P-P1.00_XUNPU_WAFER-SH1.0-2PWB -> Rick_Connector:CONN-SMD_2P-P1.00_XUNPU_WAFER-SH1.0-2PWB
- U5: value CAN -> WAFER-SH1.0-2PWB; footprint Library:CONN-SMD_2P-P1.00_XUNPU_WAFER-SH1.0-2PWB -> Rick_Connector:CONN-SMD_2P-P1.00_XUNPU_WAFER-SH1.0-2PWB
- U6: footprint Library:TJA1051T31J_SOIC-8_L4.9-W3.9-P1.27-LS6.0-BL -> Rick_CAN:TJA1051T31J_SOIC-8_L4.9-W3.9-P1.27-LS6.0-BL
- U7: footprint Library:BQ7692003PW_TSSOP-20_L6.5-W4.4-P0.65-LS6.4-BL -> Rick_BMS:BQ7692003PW_TSSOP-20_L6.5-W4.4-P0.65-LS6.4-BL
- U8: footprint Library:TPS5450DDAR -> Rick_Power:TPS5450DDAR
- U9: footprint Library:TLV76733DRVR_SON65P200X200X80-7N -> Rick_Regulator_Linear:TLV76733DRVR_SON65P200X200X80-7N
- X1: value Crystal_16MHz_15pF_3P -> CSTCE16M0V53-R0; footprint Library:Crystal_SMD3213-3P -> Rick_Crystal:Crystal_SMD3213-3P
- XTAL1: value Q13FC1350000400 -> Q13FC13500004; footprint Library:Q13FC1350000400 -> Rick_Crystal:Q13FC13500004
- moved R37 13.6 mm to (137.8, 110.5)
- moved C23 12.6 mm to (136.0, 108.7)
- moved R33 11.6 mm to (134.2, 110.5)
- moved C17 6.28 mm to (132.8, 112.8), turned to 0 degrees
- moved Q1 5.84 mm to (126.0, 99.3)
- moved Q2 5.84 mm to (126.0, 102.1)
- moved Q3 5.84 mm to (126.0, 104.9)
- moved Q4 5.84 mm to (126.0, 107.7)
- moved Q5 5.84 mm to (126.0, 110.5)
- moved R19 5.84 mm to (130.0, 98.5)
- moved R20 5.84 mm to (130.0, 99.9)
- moved R21 5.84 mm to (130.0, 101.3)
- moved R22 5.84 mm to (130.0, 102.7)
- moved R23 5.84 mm to (130.0, 104.2)
- moved R24 5.84 mm to (130.0, 105.6)
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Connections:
- C22 pad 2: /BQ76920/SRN -> /BQ76920/SRP
- C23 pad 1: /BQ76920/SRN -> /BQ76920/SRP
- C23 pad 2: /BQ76920/SRP -> /BQ76920/SRN
- C24 pad 1: /BQ76920/SRP -> /BQ76920/SRN
- R33 pad 2: /BQ76920/SRN -> /BQ76920/SRP
- R37 pad 2: /BQ76920/SRP -> /BQ76920/SRN
- R48 pad 2: PACK+ -> PACK-
- R49 pad 1: PACK- -> GND
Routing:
- net GND: track 86.7 -> 63.8 mm, vias 64 -> 71
- net /BQ76920/SRP: track 25.5 -> 6.96 mm
- net /BQ76920/SRN: track 24.9 -> 6.62 mm
- net -BATT: track 14.0 -> 30.6 mm
- net Net-(C26-Pad1): track 18.9 -> 31.9 mm
- net +5V: track 57.3 -> 44.6 mm, vias 2 -> 23
- net Net-(D8-A): track 17.0 -> 25.5 mm
- net PACK+: track 28.6 -> 20.7 mm, vias 4 -> 5
- net Net-(D7-A): track 15.1 -> 22.1 mm
- net /BQ76920/VC4: track 15.6 -> 9.25 mm
- net Net-(D6-A): track 13.4 -> 19.4 mm
- net /BQ76920/VC1: track 57.4 -> 51.5 mm
- net /BQ76920/VC3: track 14.5 -> 8.98 mm
- net /BQ76920/VC2: track 14.9 -> 9.51 mm
- net /BQ76920/VC5: track 13.1 -> 7.78 mm
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- added copper zone on B.Cu, net +5V
- added copper zone on In2.Cu, net +5V
- added copper zone on F.Cu, net Net-(Q1-D)
- added copper zone on F.Cu, net Net-(Q11-S)
- added copper zone on F.Cu, net Net-(Q2-D)
- added copper zone on F.Cu, net Net-(Q3-D)
- added copper zone on F.Cu, net Net-(Q4-D)
- added copper zone on F.Cu, net Net-(Q5-D)
- added copper zone on B.Cu, net Net-(U8-BOOT)
